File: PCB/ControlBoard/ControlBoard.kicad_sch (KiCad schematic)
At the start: 28 parts, among them J1 ICSP, J3 Bus, J4 Submodule A, J5 Submodule B, J6 Submodule C, SW1 Boot, U1 PIC18F57Q84, U2 MCP2562-E-SN, U7 CM1293A‐04SO

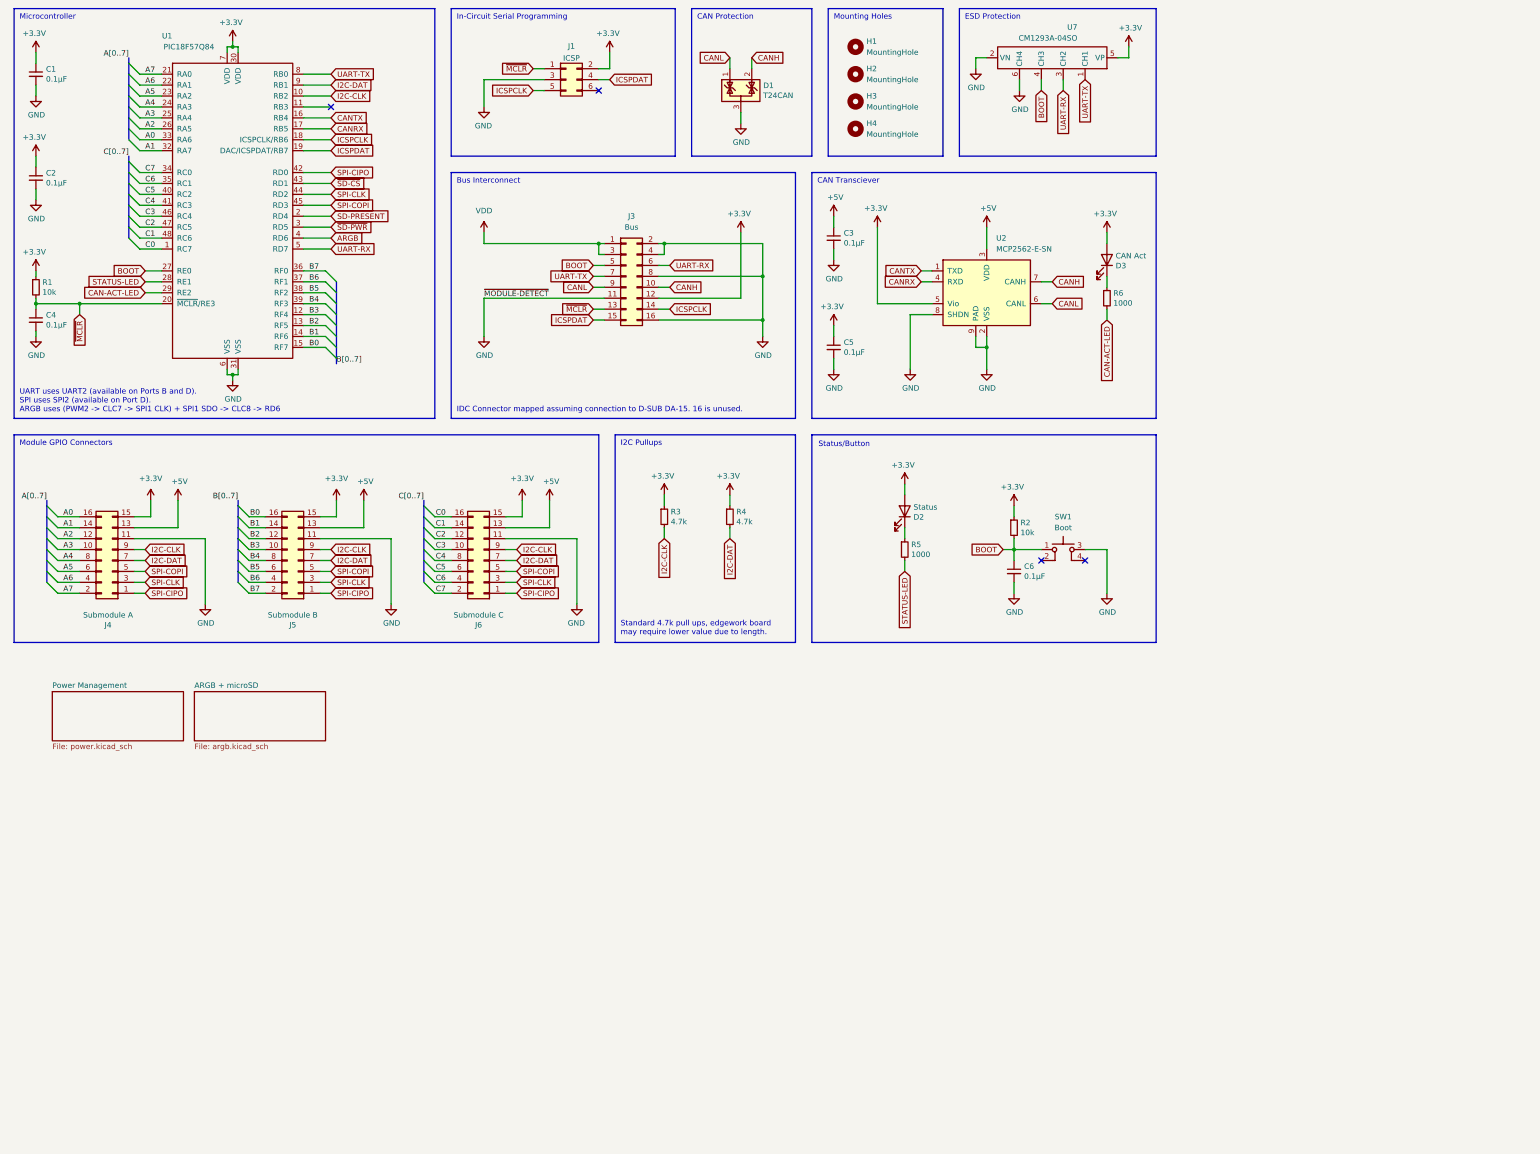
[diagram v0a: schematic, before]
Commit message: feat: Rework ControlBoard to use an STM32H562VGT6.
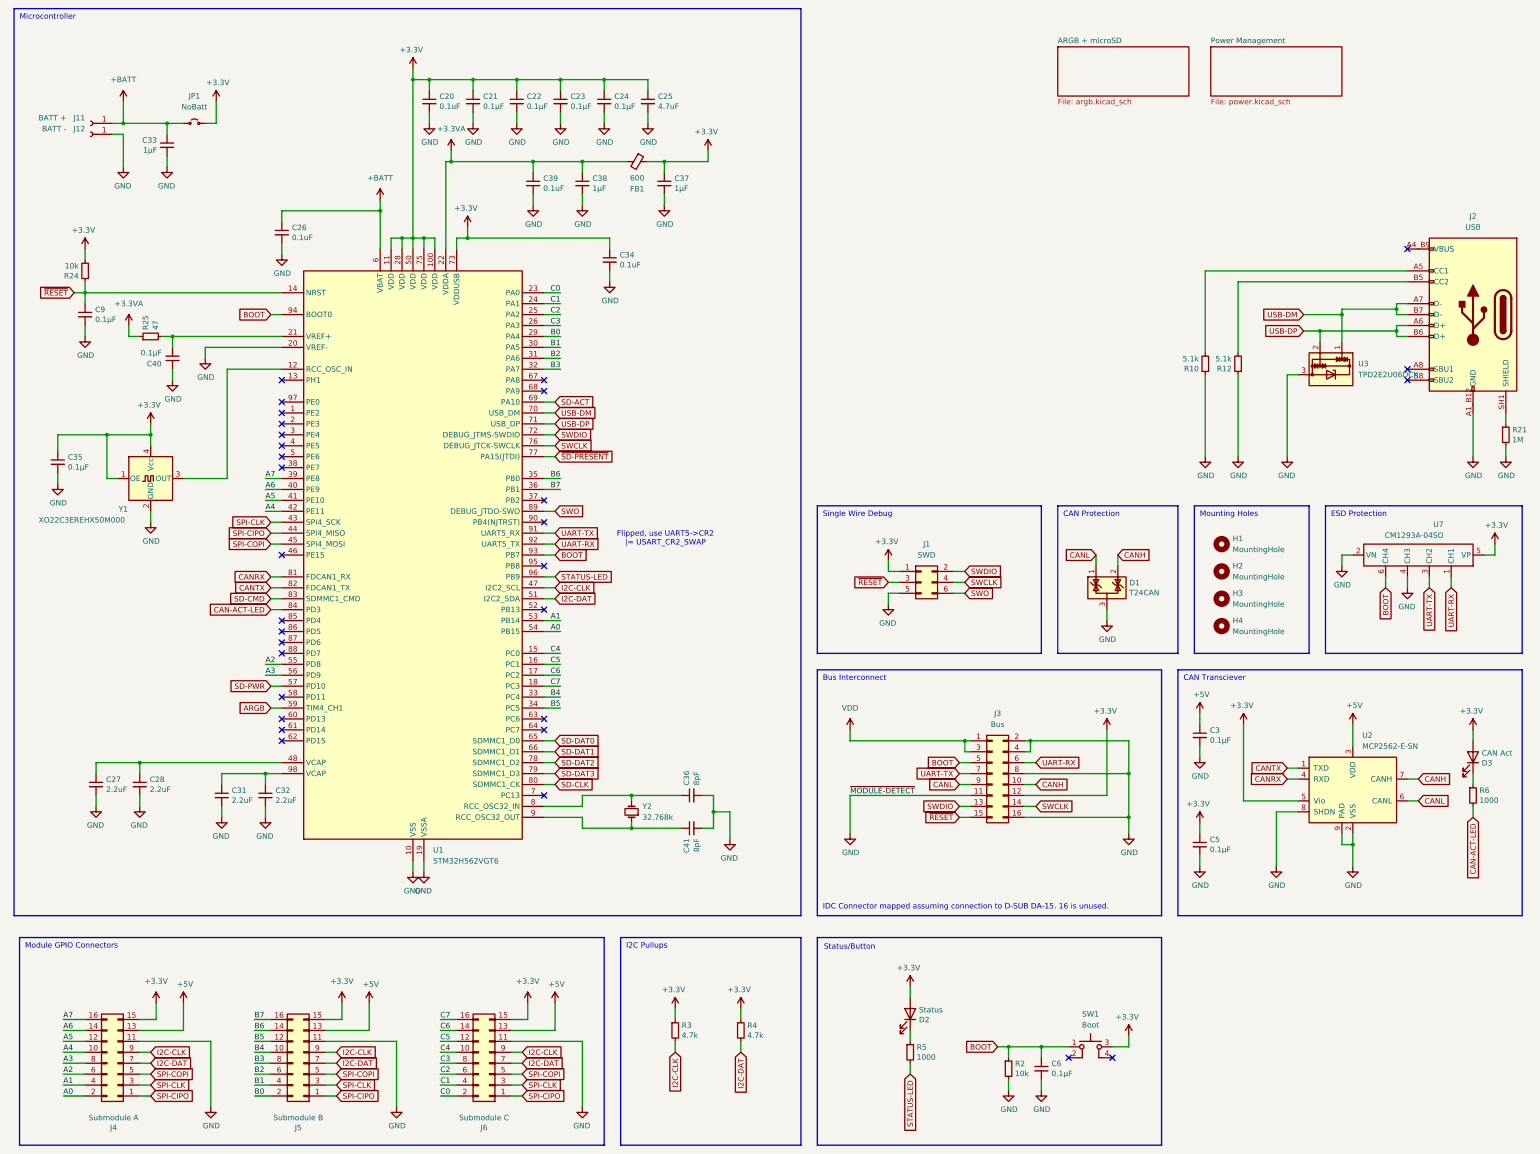
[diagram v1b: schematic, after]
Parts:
- removed C1, C2, C4: 0.1μF, Capacitor_SMD:C_0603_1608Metric, symbol Device:C_Small
- removed R1: 10k, Resistor_SMD:R_0603_1608Metric, symbol Device:R_Small
- removed U1: PIC18F57Q84, Package_QFP:TQFP-48_7x7mm_P0.5mm, symbol KTANE:PIC18F57Q84
- added C20, C26, C34, C39: 0.1uF, Capacitor_SMD:C_0603_1608Metric, symbol Device:C_Small
- added C21, C22, C23, C24, C35, C40, C9: 0.1μF, Capacitor_SMD:C_0603_1608Metric, symbol Device:C_Small
- added C25: 4.7uF, Capacitor_SMD:C_0603_1608Metric, symbol Device:C_Small
- added C27, C28, C31, C32: 2.2uF, Capacitor_SMD:C_0603_1608Metric, symbol Device:C_Small
- added C33, C37, C38: 1μF, Capacitor_SMD:C_0603_1608Metric, symbol Device:C_Small
- added C36, C41: 8pF, Capacitor_SMD:C_0603_1608Metric, symbol Device:C_Small
- added FB1: 600, Inductor_SMD:L_0603_1608Metric, symbol Device:FerriteBead_Small
- added J11: BATT +, KTANE:Pad4x2, symbol Connector:Conn_01x01_Socket
- added J12: BATT -, KTANE:Pad4x2, symbol Connector:Conn_01x01_Socket
- added J2: USB, KTANE:SAMESKY_UJ20-C-H-G-SMT-1A-P16-TR, symbol KTANE:USB_C_Receptacle_USB2.0_16P_CombinedPins
- added JP1: NoBatt, Jumper:SolderJumper-2_P1.3mm_Open_Pad1.0x1.5mm, symbol Jumper:Jumper_2_Small_Open
- added R10, R12: 5.1k, Resistor_SMD:R_0603_1608Metric, symbol Device:R_Small
- added R21: 1M, Resistor_SMD:R_0603_1608Metric, symbol Device:R_Small
- added R24: 10k, Resistor_SMD:R_0603_1608Metric, symbol Device:R_Small
- added R25: 47, Resistor_SMD:R_0603_1608Metric, symbol Device:R_Small
- added U1: STM32H562VGT6, Package_QFP:LQFP-100_14x14mm_P0.5mm, symbol MCU_ST_STM32H5:STM32H562VGTx
- added U3: TPD2E2U06DCK, Package_TO_SOT_SMD:SOT-323_SC-70, symbol Power_Protection:TPD2E2U06DCK
- added Y1: XO22C3EREHX50M000, KTANE:Oscillator_SMD-Vishay_X022C_2.5mmx2.0mm, symbol KTANE:DSC60XX
- added Y2: 32.768k, Crystal:Crystal_SMD_2012-2Pin_2.0x1.2mm, symbol Device:Crystal_Small
- H1, H2, H3, H4: footprint MountingHole:MountingHole_3.2mm_M3 -> KTANE:MountingHole_3.2mm_M3_NoCopper
- J1: value ICSP -> SWD
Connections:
- net +3.3V: now also J1.1 (Pin_1), SW1.3, C20.1, C21.1, C22.1, C23.1, C24.1, C25.1, C34.1, C35.1, C37.1, FB1.1, JP1.1 (A), R24.2, U1.100 (VDD), U1.11 (VDD), U1.28 (VDD), U1.50 (VDD), U1.73 (VDDUSB), U1.75 (VDD), Y1.1 (OE), Y1.4 (Vcc); no longer J1.2 (Pin_2), R2.1
- net A0: now also J4.2 (Pin_2), U1.54 (PB15); no longer J4.16 (Pin_16)
- net A1: now also J4.4 (Pin_4), U1.53 (PB14); no longer J4.14 (Pin_14)
- net A2: now also J4.6 (Pin_6), U1.55 (PD8); no longer J4.12 (Pin_12)
- net A3: now also J4.8 (Pin_8), U1.56 (PD9); no longer J4.10 (Pin_10)
- net A4: now also J4.10 (Pin_10), U1.42 (PE11); no longer J4.8 (Pin_8)
- net A5: now also J4.12 (Pin_12), U1.41 (PE10); no longer J4.6 (Pin_6)
- net A6: now also J4.14 (Pin_14), U1.40 (PE9); no longer J4.4 (Pin_4)
- net A7: now also J4.16 (Pin_16), U1.39 (PE8); no longer J4.2 (Pin_2)
- net ARGB: now also U1.59 (PD12)
- net B0: now also J5.2 (Pin_2), U1.29 (PA4); no longer J5.16 (Pin_16)
- net B1: now also J5.4 (Pin_4), U1.30 (PA5); no longer J5.14 (Pin_14)
- net B2: now also J5.6 (Pin_6), U1.31 (PA6); no longer J5.12 (Pin_12)
- net B3: now also J5.8 (Pin_8), U1.32 (PA7); no longer J5.10 (Pin_10)
- net B4: now also J5.10 (Pin_10), U1.33 (PC4); no longer J5.8 (Pin_8)
- net B5: now also J5.12 (Pin_12), U1.34 (PC5); no longer J5.6 (Pin_6)
- net B6: now also J5.14 (Pin_14), U1.35 (PB0); no longer J5.4 (Pin_4)
- net B7: now also J5.16 (Pin_16), U1.36 (PB1); no longer J5.2 (Pin_2)
- net BOOT: now also R2.1, U7.6 (CH4), U1.93 (PB7), U1.94 (BOOT0); no longer R2.2, U7.4 (CH3)
- net C0: now also J6.2 (Pin_2), U1.23 (PA0); no longer J6.16 (Pin_16)
- net C1: now also J6.4 (Pin_4), U1.24 (PA1); no longer J6.14 (Pin_14)
- net C2: now also J6.6 (Pin_6), U1.25 (PA2); no longer J6.12 (Pin_12)
- net C3: now also J6.8 (Pin_8), U1.26 (PA3); no longer J6.10 (Pin_10)
- net C4: now also J6.10 (Pin_10), U1.15 (PC0); no longer J6.8 (Pin_8)
- net C5: now also J6.12 (Pin_12), U1.16 (PC1); no longer J6.6 (Pin_6)
- net C6: now also J6.14 (Pin_14), U1.17 (PC2); no longer J6.4 (Pin_4)
- net C7: now also J6.16 (Pin_16), U1.18 (PC3); no longer J6.2 (Pin_2)
- net CAN-ACT-LED: now also U1.84 (PD3)
- net CANRX: now also U1.81 (PD0)
- net CANTX: now also U1.82 (PD1)
- net GND: now also J1.5 (Pin_5), R2.2, U7.4 (CH3), C20.2, C21.2, C22.2, C23.2, C24.2, C25.2, C26.2, C27.2, C28.2, C31.2, C32.2, C33.2, C34.2, C35.2, C36.2, C37.2, C38.2, C39.2, C40.1, C41.2, C9.2, J12.1 (Pin_1), J2.A1_B12 (GND), J2.B1_A12 (GND), R10.1, R12.1, R21.2, U1.10 (VSS), U1.19 (VSSA), U1.20 (VREF-), U1.27 (VSS), U1.49 (VSS), U1.74 (VSS), U1.99 (VSS), U3.3, Y1.2 (GND); no longer J1.3 (Pin_3), SW1.3, U7.6 (CH4)
- net I2C-CLK: now also U1.47 (PB10)
- net I2C-DAT: now also U1.51 (PB12)
- net SPI-CIPO: now also U1.44 (PE13)
- net SPI-CLK: now also U1.43 (PE12)
- net SPI-COPI: now also U1.45 (PE14)
- net STATUS-LED: now also U1.96 (PB9)
- net UART-RX: now also U7.1 (CH1), U1.92 (PB6); no longer U7.3 (CH2)
- net UART-TX: now also U7.3 (CH2), U1.91 (PB5); no longer U7.1 (CH1)
- net SWO: now reaches J1.6 (Pin_6)
- net SWO: now also U1.89 (PB3(JTDO)
- net ICSPCLK renamed SWCLK
- net SWCLK: now also J1.4 (Pin_4), U1.76 (PA14(JTCK); no longer J1.5 (Pin_5)
- net ICSPDAT renamed ~{RESET}
- net ~{RESET}: now also J1.3 (Pin_3), C9.1, R24.1, U1.14 (NRST); no longer J1.4 (Pin_4)
- net ~{MCLR} renamed SWDIO
- net SWDIO: now also J1.2 (Pin_2), U1.72 (PA13(JTMS); no longer J1.1 (Pin_1)
- new net: C27.1, C28.1, U1.48 (VCAP)
- new net: U1.12 (PH0), Y1.3 (OUT)
- new net: J2.A4_B9 (VBUS), J2.B4_A9 (VBUS)
- new net: J2.A5 (CC1), R10.2
- new net: J2.B5 (CC2), R12.2
- new net: J2.SH1 (SHIELD), R21.1
- new net: J2.SH2 (SHIELD), J2.SH3 (SHIELD), J2.SH4 (SHIELD)
- new net: C40.2, R25.2, U1.21 (VREF+)
- new net: C41.1, U1.9 (PC15), Y2.1
- new net: C36.1, U1.8 (PC14), Y2.2
- new net: C31.1, C32.1, U1.98 (VCAP)
- new net +3.3VA: C38.1, C39.1, FB1.2, R25.1, U1.22 (VDDA)
- new net +BATT: C26.1, C33.1, J11.1 (Pin_1), JP1.2 (B), U1.6 (VBAT)
- new net SD-ACT: U1.69 (PA10)
- new net SD-CLK: U1.80 (PC12)
- new net SD-CMD: U1.83 (PD2)
- new net SD-DAT0: U1.65 (PC8)
- new net SD-DAT1: U1.66 (PC9)
- new net SD-DAT2: U1.78 (PC10)
- new net SD-DAT3: U1.79 (PC11)
- new net SD-PWR: U1.57 (PD10)
- new net USB-DM: J2.A7 (D-), J2.B7 (D-), U1.70 (PA11), U3.1
- new net USB-DP: J2.A6 (D+), J2.B6 (D+), U1.71 (PA12), U3.2
- new net ~{SD-PRESENT}: U1.77 (PA15(JTDI))
- no-connect marks 4 -> 31
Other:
- note added: "Flipped, use UART5->CR2 |= USART_CR2_SWAP"
- note added: "Single Wire Debug"
- note removed: "In-Circuit Serial Programming"
- note removed: "Standard 4.7k pull ups, edgework board may require lower value due to length."
- note removed: "UART uses UART2 (available on Ports B and D). SPI uses SPI2 (available on Port D). ARGB uses (PWM2 -> CLC7 -> SPI1 CLK) + SPI1 SDO -> CLC8 -> RD6"
- moved on the sheet: C3, C5, C6, D1, D2, D3, H1, H2, H3, H4, J1, J3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

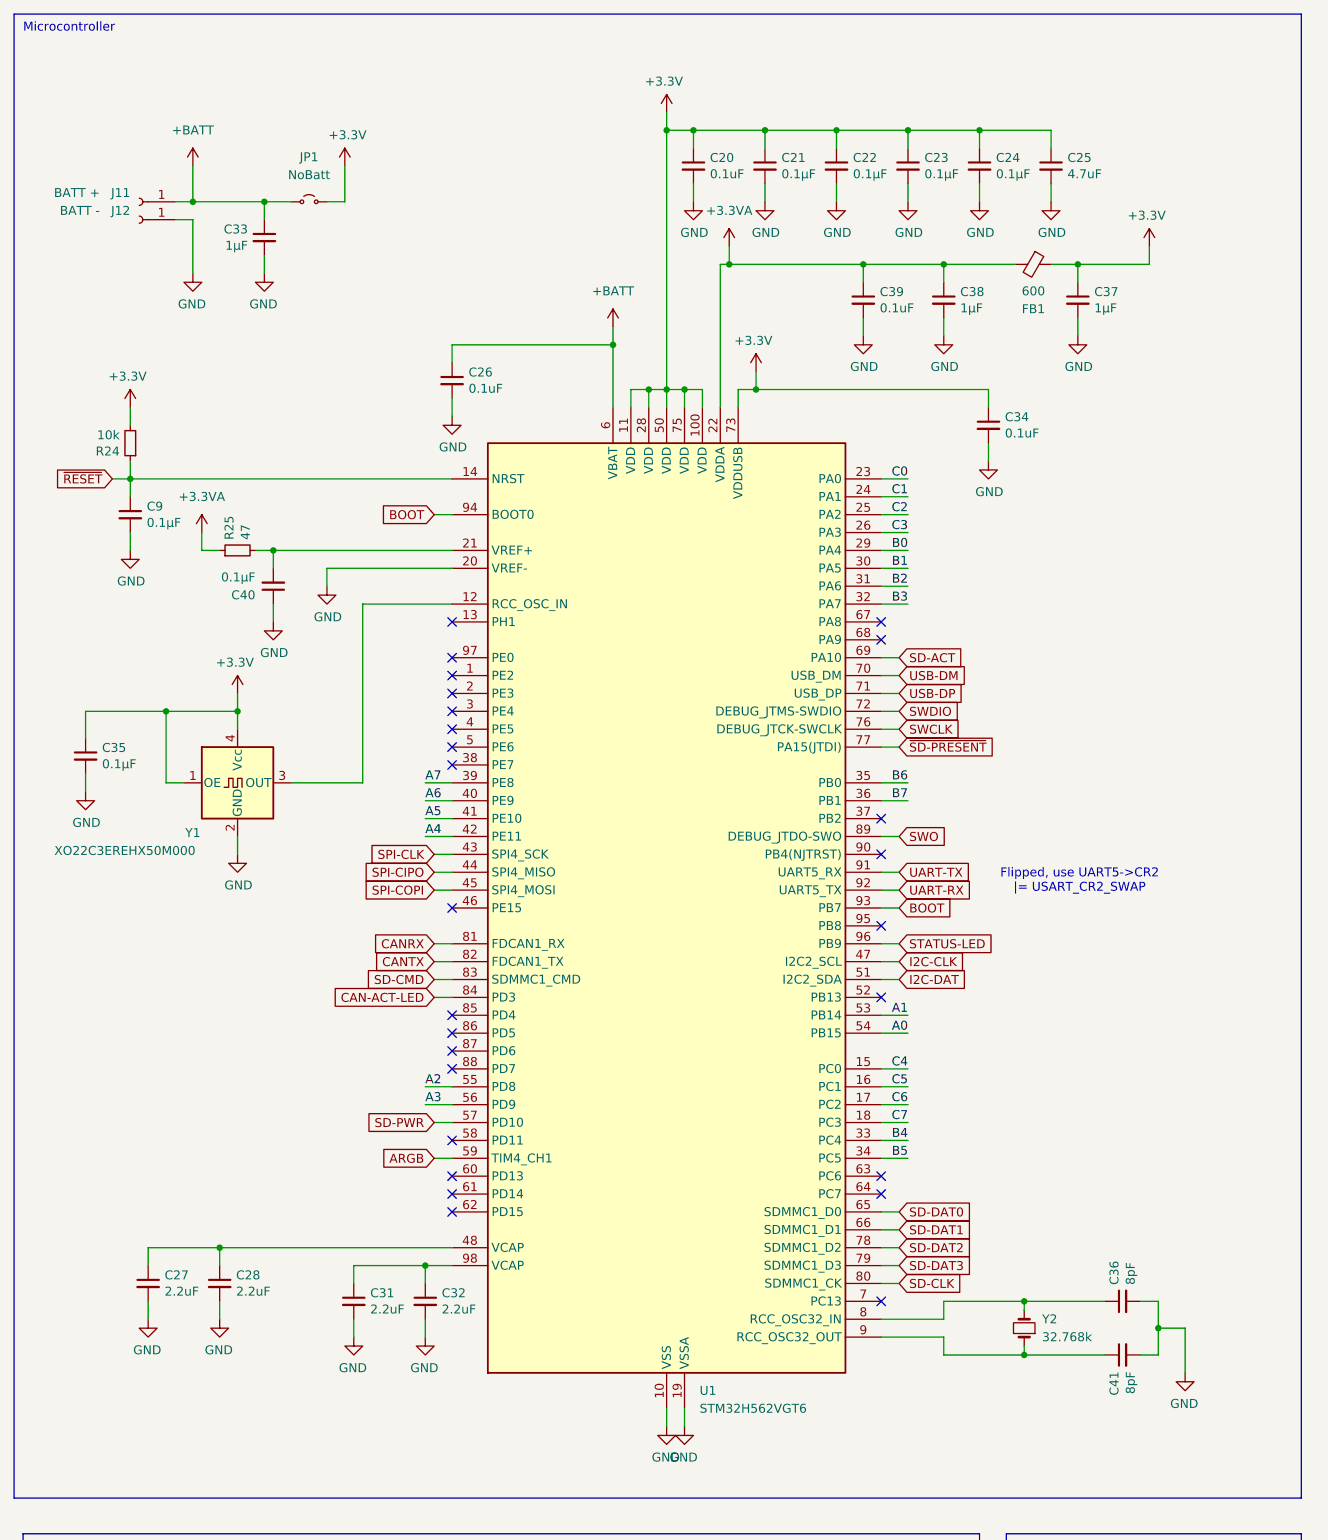
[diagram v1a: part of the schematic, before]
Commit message: feat: Remove backup battery for RTC, and crystal. 1PPS can be derived from HSE.
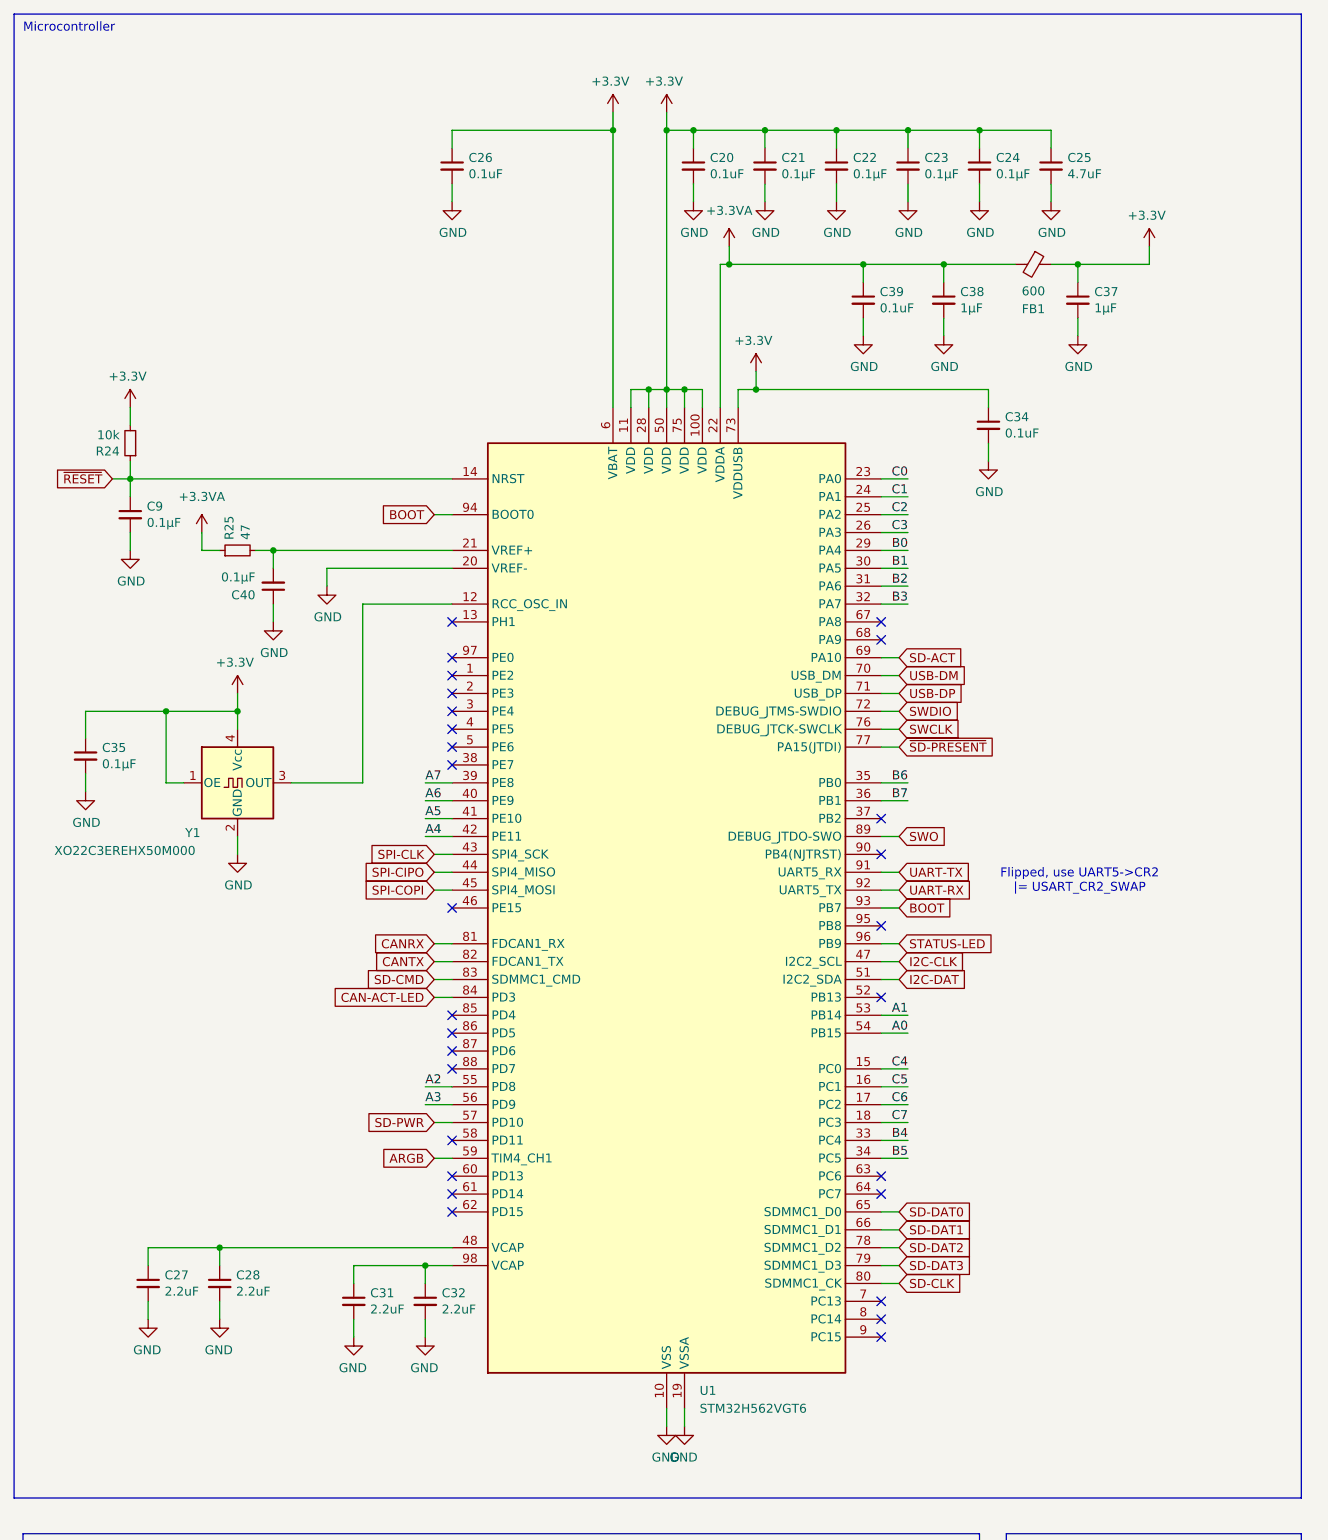
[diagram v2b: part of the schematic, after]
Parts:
- removed C33: 1μF, Capacitor_SMD:C_0603_1608Metric, symbol Device:C_Small
- removed C36, C41: 8pF, Capacitor_SMD:C_0603_1608Metric, symbol Device:C_Small
- removed J11: BATT +, KTANE:Pad4x2, symbol Connector:Conn_01x01_Socket
- removed J12: BATT -, KTANE:Pad4x2, symbol Connector:Conn_01x01_Socket
- removed JP1: NoBatt, Jumper:SolderJumper-2_P1.3mm_Open_Pad1.0x1.5mm, symbol Jumper:Jumper_2_Small_Open
- removed Y2: 32.768k, Crystal:Crystal_SMD_2012-2Pin_2.0x1.2mm, symbol Device:Crystal_Small
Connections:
- net +BATT is gone; now on net +3.3V: C26.1, U1.6 (VBAT)
- no-connect marks 31 -> 33
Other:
- moved on the sheet: C26
